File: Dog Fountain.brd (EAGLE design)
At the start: 88.6 x 53.3 mm, 19 parts, among them IC1 L298, J1 22-27-2021-02, J4 22-27-2021-02

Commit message: PCB board first test
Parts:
- D1, D2, D3, D4: device diode:DO41-10 -> diode:DO41-7.6
- R1, R3: value (none) -> 100 Ω
- R2: value (none) -> 180 Ω
- moved JP4 71.2 mm to (83.8, 45.7), turned to 0 degrees
- moved U$1 31.4 mm to (43.2, 35.6), turned to 270 degrees
- moved D5 27.5 mm to (20.3, 5.08), turned to 0 degrees
- moved R2 22.2 mm to (22.9, 11.4), turned to 270 degrees
- moved R1 18.8 mm to (20.3, 11.4), turned to 270 degrees
- moved J4 17.8 mm to (86.4, 8.89)
- moved R3 15.3 mm to (17.8, 11.4), turned to 270 degrees
- moved D1 9.25 mm to (76.2, 36.8)
- moved J1 8.89 mm to (86.4, 29.2)
- moved C1 7.18 mm to (50.8, 12.7)
- moved D3 6.84 mm to (76.2, 26.7)
- moved D2 6.35 mm to (73.7, 34.3)
- moved B3 5.68 mm to (71.1, 8.26)
- moved B4 5.68 mm to (78.7, 8.26)
- moved IC1 5.24 mm to (58.4, 26.7)
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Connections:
- net N$11: now also U$1.D7; no longer U$1.D13
- net N$12: now also U$1.D6; no longer U$1.D8
- net N$13: now also U$1.D5; no longer U$1.D7
- net N$14: now also U$1.A5; no longer U$1.D9
- net N$15: now also U$1.A4; no longer U$1.D10
- net N$16: now also U$1.A3; no longer U$1.D11
- net N$5: now also U$1.D2; no longer U$1.D4
- net N$8: now also U$1.D4; no longer U$1.D2
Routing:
- net N$11: track 9.72 -> 73.8 mm
- net GND: track 272.0 -> 238.8 mm, vias 0 -> 4
- net +24V: track 88.6 -> 62.8 mm, vias 0 -> 3
- net N$15: track 27.1 -> 7.62 mm
- net N$14: track 27.1 -> 7.62 mm
- net N$16: track 27.1 -> 7.62 mm
- net N$12: track 18.4 -> 33.9 mm
- net N$10: track 27.5 -> 15.2 mm
- net N$9: track 26.3 -> 15.4 mm
- net N$8: track 21.8 -> 30.0 mm
- net +5V: track 122.9 -> 117.5 mm, vias 2 -> 3
- net N$13: track 22.0 -> 27.1 mm
- net N$3: track 13.3 -> 8.52 mm
- net N$4: track 28.2 -> 32.1 mm
- net N$5: track 21.5 -> 23.9 mm
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
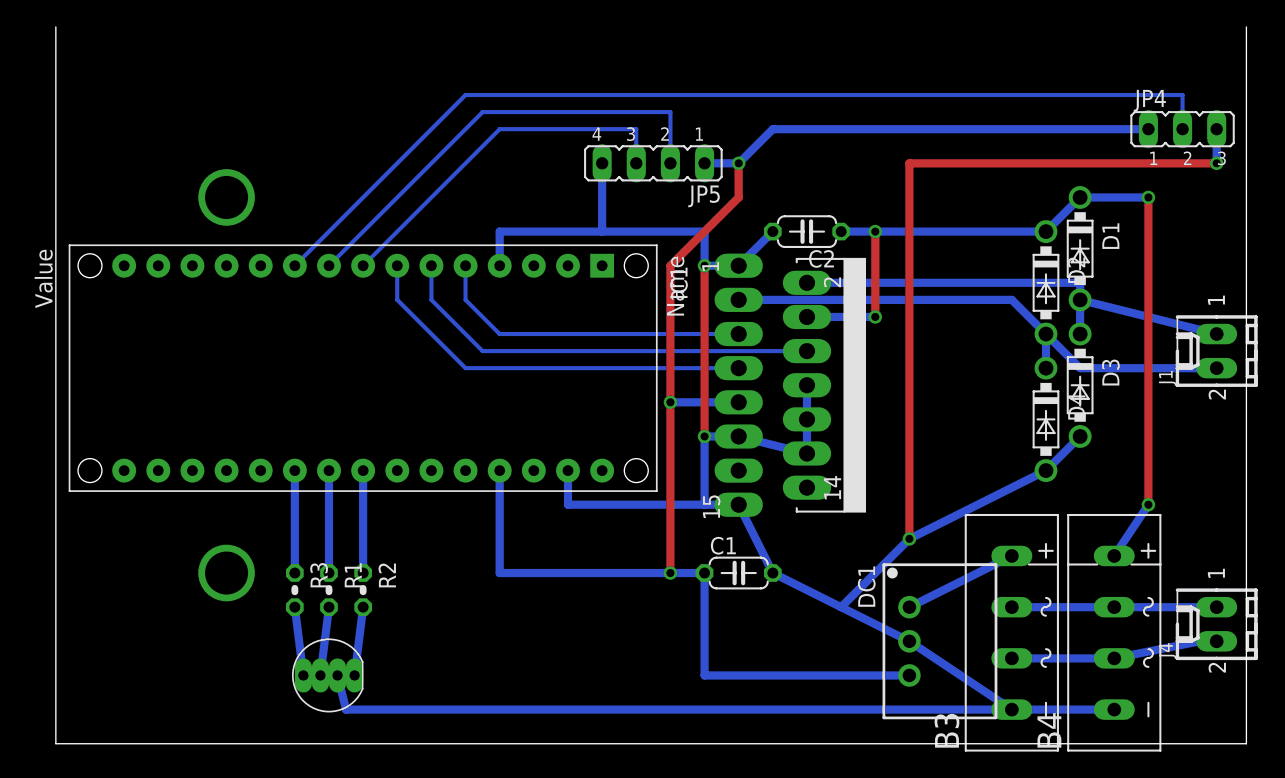
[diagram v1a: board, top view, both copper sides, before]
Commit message: Another try with 12v power supply
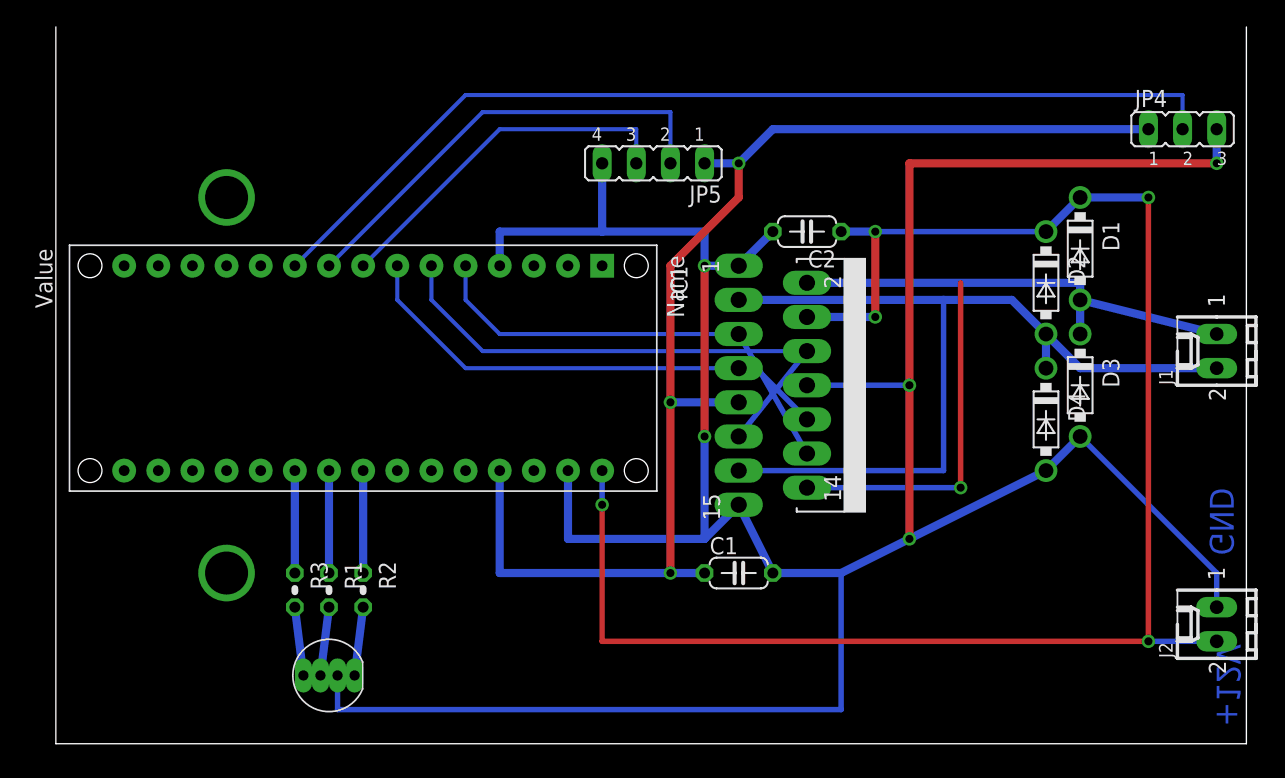
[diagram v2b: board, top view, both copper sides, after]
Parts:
- removed B3, B4: RECTIFIER-2KBP, rectifier:2KBP
- removed DC1: R-78C5.0-1.0, dc-dc-converter:SIP3
- renumbered J4 to J2
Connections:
- removed net +24V: B4.+, C2.1, D1.C, D2.C, IC1.4
- removed net N$10: B3.AC2, B4.AC2, J2.1
- removed net N$3: B3.+, DC1.1
- removed net N$9: B3.AC1, B4.AC1, J2.2
- new net +12V: C2.1, D1.C, D2.C, IC1.4, J2.2, U$1.VIN
- net +5V: no longer DC1.3
- net GND: now also J2.1; no longer B3.-, B4.-, DC1.2, IC1.10, IC1.11, IC1.12
- net N$4: now also IC1.11
- net N$5: now also IC1.12
- net N$6: now also IC1.13
- net N$7: now also IC1.14
- net N$8: now also IC1.10
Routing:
- net +12V: track 0.00 -> 126.8 mm, vias 0 -> 4
- net +24V: track 62.8 -> 0.00 mm, vias 3 -> 0
- net N$6: track 40.2 -> 68.1 mm
- net N$7: track 34.6 -> 61.3 mm, vias 0 -> 1
- net +5V: track 117.5 -> 94.6 mm
- net N$9: track 15.4 -> 0.00 mm
- net N$10: track 15.2 -> 0.00 mm
- net N$5: track 23.9 -> 34.2 mm
- net GND: track 238.8 -> 230.1 mm, vias 4 -> 5
- net N$3: track 8.52 -> 0.00 mm
- net N$4: track 32.1 -> 40.2 mm
- net N$8: track 30.0 -> 36.7 mm
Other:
- board text added: "+12V"
- board text added: "GND"
